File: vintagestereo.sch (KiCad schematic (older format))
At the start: 62 parts, among them J1 Conn_01x08_Male, U1 TL074, U2 TL074

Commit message: autosync
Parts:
- added U?: RDA5807M, symbol AA-ROBSCH:RDA5807M
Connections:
- net labels added: VDD
- wire segments 71 -> 74
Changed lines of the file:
@@
 L power:+5V #PWR?
 U 1 1 609BDE55
-P 10750 4050
-F 0 "#PWR?" H 10750 3900 50  0001 C CNN
-F 1 "+5V" V 10765 4178 50  0000 L CNN
-F 2 "" H 10750 4050 50  0001 C CNN
-F 3 "" H 10750 4050 50  0001 C CNN
-	1    10750 4050
+P 10800 4050
+F 0 "#PWR?" H 10800 3900 50  0001 C CNN
+F 1 "+5V" V 10815 4178 50  0000 L CNN
+F 2 "" H 10800 4050 50  0001 C CNN
+F 3 "" H 10800 4050 50  0001 C CNN
+	1    10800 4050
 	0    1    1    0
 $EndComp
@@
 Text GLabel 8900 5500 0    50   Input ~ 0
 Amp-R
+Text GLabel 2300 3650 3    50   Output ~ 0
+Pre-AL
+Text GLabel 2200 3650 3    50   Output ~ 0
+Pre-AR
+$Comp
+L power:GND #PWR?
+U 1 1 609E4103
+P 2300 2850
+F 0 "#PWR?" H 2300 2600 50  0001 C CNN
+F 1 "GND" H 2305 2677 50  0000 C CNN
+F 2 "" H 2300 2850 50  0001 C CNN
+F 3 "" H 2300 2850 50  0001 C CNN
+	1    2300 2850
+	-1   0    0    1
+$EndComp
+$Comp
+L power:GND #PWR?
+U 1 1 609E6149
+P 2100 2850
+F 0 "#PWR?" H 2100 2600 50  0001 C CNN
+F 1 "GND" H 2105 2677 50  0000 C CNN
+F 2 "" H 2100 2850 50  0001 C CNN
+F 3 "" H 2100 2850 50  0001 C CNN
+	1    2100 2850
+	-1   0    0    1
+$EndComp
+$Comp
+L power:GND #PWR?
+U 1 1 609E6DD9
+P 2100 3650
+F 0 "#PWR?" H 2100 3400 50  0001 C CNN
+F 1 "GND" H 2105 3477 50  0000 C CNN
+F 2 "" H 2100 3650 50  0001 C CNN
+F 3 "" H 2100 3650 50  0001 C CNN
+	1    2100 3650
+	1    0    0    -1
+$EndComp
+Wire Wire Line
+	10800 4050 10750 4050
+Connection ~ 10750 4050
+Wire Wire Line
+	10750 4050 10750 4200
+Wire Wire Line
+	10750 4200 10850 4200
+Text GLabel 10850 4200 2    50   Output Italic 0
+VDD
+Text GLabel 2000 3650 3    50   Input Italic 0
+VDD
+$Comp
+L AA-ROBSCH:RDA5807M U?
+U 1 1 609DFFD6
+P 2050 3200
+F 0 "U?" H 2378 3196 50  0000 L CNN
+F 1 "RDA5807M" H 2378 3105 50  0000 L CNN
+F 2 "" H 2000 3300 50  0001 C CNN
+F 3 "" H 2000 3300 50  0001 C CNN
+	1    2050 3200
+	1    0    0    -1
+$EndComp
 $EndSCHEMATC

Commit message: autosync
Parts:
- removed C? (x12): .1uf, symbol Device:CP
- removed C? (x2): 100uf, symbol Device:CP
- removed C? (x6): 10uf, symbol Device:CP
- removed R? (x6): 1K, symbol Device:R
- removed R? (x12): 47K, symbol Device:R
- removed R? (x6): 100K, symbol Device:R
- removed R? (x2): 10R, symbol Device:R
- removed RV? (x5): 10K A, symbol Device:R_POT_Dual_Separate
- removed unit 5 of U1
- removed unit 3 of U1
- removed unit 4 of U1
- removed unit 2 of U1
- removed U2: TL074, symbol Amplifier_Operational:TL074
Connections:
- net labels added: Pre-CL, Pre-CR
- wire segments 74 -> 20

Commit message: autosync
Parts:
- removed RV?: 10K A, symbol Device:R_POT_Dual_Separate
- added A?: Arduino_Nano_v3.x, Module:Arduino_Nano, symbol MCU_Module:Arduino_Nano_v3.x
- added J? (x2): Conn_01x02_Female, symbol Connector:Conn_01x02_Female
- added J?: Conn_01x04_Female, symbol Connector:Conn_01x04_Female
- added J?: AudioJack2_Ground, symbol Connector:AudioJack2_Ground
- added RV? (x3): R_POT_Dual, symbol Device:R_POT_Dual
- added SW? (x5): SW_Push, symbol Switch:SW_Push
- added SW?: Rotary_Encoder_Switch, symbol Device:Rotary_Encoder_Switch
- U1: value TL074 -> BLUE MODULE
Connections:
- net +5V: now also J1.6 (Pin_6), R?.2, U1.17 (VCC), U1.22 (VCC), A?.27 (+5V), J?.3 (Pin_3), SW?.2, SW?.2, SW?.2, SW?.2, SW?.2, SW?.S1; no longer U?.7 (SCL)
- net GND: now also A?.29 (GND), A?.4 (GND), J?.2 (Pin_2), J?.4 (Pin_4), J?.G, RV?.3, RV?.3, RV?.3, RV?.6, RV?.6, RV?.6, SW?.C; no longer U?.3 (LOut), U?.8 (N/C)
- net Mute: now also A?.20 (A1)
- net Pre-AL: now also U?.3 (LOut), RV?.1; no longer U?.10 (VCC), U?.12 (X0)
- net Pre-AR: now also U?.2 (ROut), RV?.4; no longer U?.1 (Y0), U?.9 (N/C)
- net Pre-BL: now also RV?.1; no longer U?.14 (X1)
- net Pre-BR: now also RV?.4; no longer U?.5 (Y1)
- net Pre-CL: now also J?.S, RV?.1; no longer U?.15 (X2)
- net Pre-CR: now also J?.T, RV?.4; no longer U?.2 (Y2)
- net at U1.1 (M+): now also J?.2 (Pin_2)
- net Vol+: now reaches U1.11 (VOL+)
- net Vol+: now also A?.12 (D9)
- net VOL-: now reaches U1.12 (VOL-)
- net VOL-: now also A?.13 (D10)
- net Next: now reaches U1.13 (NEXT)
- net Next: now also A?.15 (D12)
- net Prev: now reaches U1.14 (PREV)
- net Prev: now also A?.16 (D13)
- net at U1.2 (M-): now also J?.1 (Pin_1)
- net at U?.5 (Antenna): now also J?.1 (Pin_1)
- net SDA: now reaches U?.6 (SDA)
- net SDA: now also A?.23 (A4), J?.1 (Pin_1)
- removed net VCC: J1.6 (Pin_6), R?.2, U1.22 (VCC)
- new net Intrp1: A?.5 (D2), SW?.A
- new net Intrp2: A?.6 (D3), SW?.B
- new net Pause: A?.14 (D11)
- new net SCL: A?.24 (A5), J?.2 (Pin_2), U?.7 (SCL)
- new net Src-AL: RV?.2, U?.12 (X0)
- new net Src-AR: RV?.5, U?.1 (Y0)
- new net Src-BL: RV?.2, U?.14 (X1)
- new net Src-BR: RV?.5, U?.5 (Y1)
- new net Src-CL: RV?.2, U?.15 (X2)
- new net Src-CR: RV?.5, U?.2 (Y2)
- new net Sw1: A?.7 (D4), SW?.1
- new net Sw2: A?.8 (D5), SW?.1
- new net Sw3: A?.9 (D6), SW?.1
- new net Sw4: A?.10 (D7), SW?.1
- new net Sw5: A?.11 (D8), SW?.1
- new net Sw6: A?.19 (A0), SW?.S2
- new net VDD: A?.17 (3V3), U?.10 (VCC)
- no-connect marks 0 -> 14

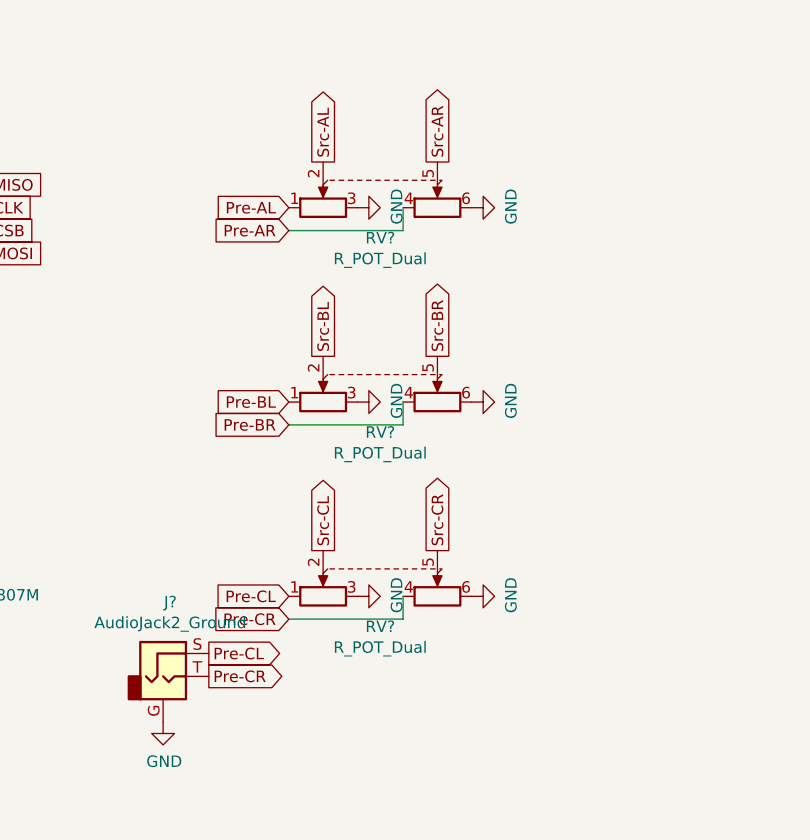
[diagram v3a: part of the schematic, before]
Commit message: swap pots
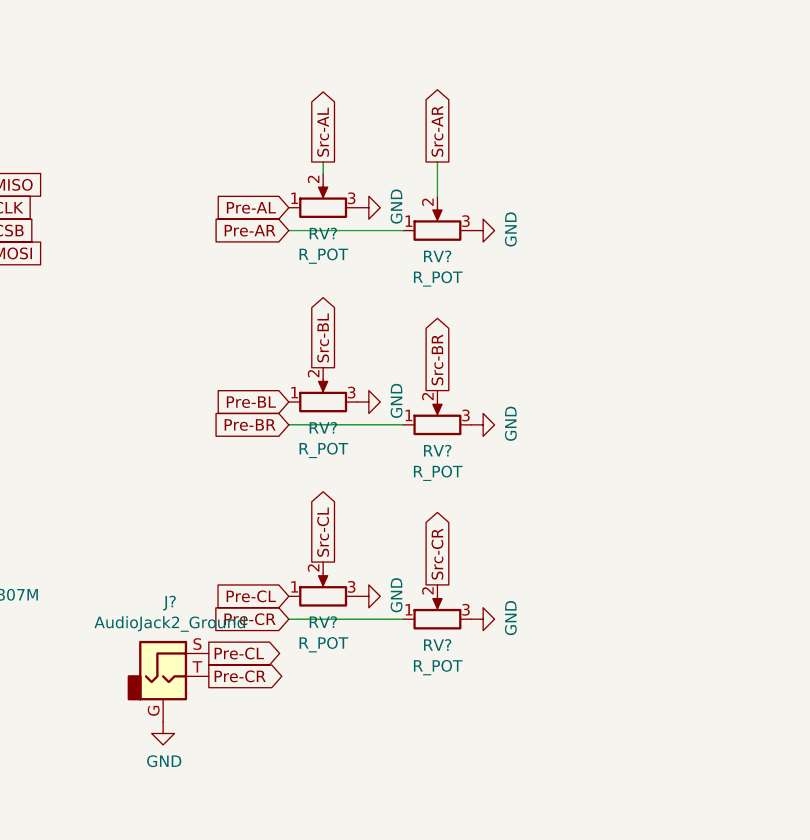
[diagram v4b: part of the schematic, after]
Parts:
- removed RV? (x3): R_POT_Dual, symbol Device:R_POT_Dual
- added RV? (x6): R_POT, symbol Device:R_POT
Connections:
- net GND: now also RV?.3, RV?.3, RV?.3, RV?.3, RV?.3, RV?.3
- net Pre-AL: now also RV?.1
- net Pre-AR: now also RV?.1
- net Pre-BL: now also RV?.1
- net Pre-BR: now also RV?.1
- net Pre-CL: now also RV?.1
- net Pre-CR: now also RV?.1
- net Src-AL: now also RV?.2
- net Src-AR: now also RV?.2
- net Src-BL: now also RV?.2
- net Src-BR: now also RV?.2
- net Src-CL: now also RV?.2
- net Src-CR: now also RV?.2
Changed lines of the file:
@@
 Text GLabel 3850 2450 0    50   Input ~ 0
 Pre-BL
-Text GLabel 4500 2250 1    50   Output ~ 0
-Src-BR
 Text GLabel 3850 2550 0    50   Input ~ 0
 Pre-BR
 Text GLabel 3850 3400 0    50   Input ~ 0
 Pre-CR
-Text GLabel 4500 3100 1    50   Output ~ 0
+Text GLabel 4500 3250 1    50   Output ~ 0
 Src-CR
-Text GLabel 4000 3100 1    50   Output ~ 0
+Text GLabel 4000 3150 1    50   Output ~ 0
 Src-CL
 Text GLabel 3850 3300 0    50   Input ~ 0
@@
 	1    0    0    -1
 $EndComp
-Text GLabel 4000 2250 1    50   Output ~ 0
+Text GLabel 4000 2300 1    50   Output ~ 0
 Src-BL
 Text GLabel 4000 1400 1    50   Output ~ 0
@@
 Pre-AL
 $Comp
-L Device:R_POT_Dual RV?
-U 1 1 60A239E4
-P 4250 1500
-F 0 "RV?" H 4250 1267 50  0000 C CNN
-F 1 "R_POT_Dual" H 4250 1176 50  0000 C CNN
-F 2 "" H 4500 1425 50  0001 C CNN
-F 3 "~" H 4500 1425 50  0001 C CNN
-	1    4250 1500
-	1    0    0    -1
-$EndComp
-Wire Wire Line
-	3850 1700 4350 1700
-Wire Wire Line
-	4350 1700 4350 1600
-$Comp
-L power:GND #PWR?
-U 1 1 60A271AB
-P 4150 1600
-F 0 "#PWR?" H 4150 1350 50  0001 C CNN
-F 1 "GND" H 4155 1427 50  0000 C CNN
-F 2 "" H 4150 1600 50  0001 C CNN
-F 3 "" H 4150 1600 50  0001 C CNN
-	1    4150 1600
-	0    -1   -1   0
-$EndComp
-$Comp
 L power:GND #PWR?
 U 1 1 60A28046
-P 4650 1600
-F 0 "#PWR?" H 4650 1350 50  0001 C CNN
-F 1 "GND" H 4655 1427 50  0000 C CNN
-F 2 "" H 4650 1600 50  0001 C CNN
-F 3 "" H 4650 1600 50  0001 C CNN
-	1    4650 1600
-	0    -1   -1   0
-$EndComp
-$Comp
-L Device:R_POT_Dual RV?
-U 1 1 60A29E30
-P 4250 2350
-F 0 "RV?" H 4250 2117 50  0000 C CNN
-F 1 "R_POT_Dual" H 4250 2026 50  0000 C CNN
-F 2 "" H 4500 2275 50  0001 C CNN
-F 3 "~" H 4500 2275 50  0001 C CNN
-	1    4250 2350
-	1    0    0    -1
-$EndComp
-Wire Wire Line
-	3850 2550 4350 2550
-Wire Wire Line
-	4350 2550 4350 2450
-$Comp
-L power:GND #PWR?
-U 1 1 60A2A0C8
-P 4150 2450
-F 0 "#PWR?" H 4150 2200 50  0001 C CNN
-F 1 "GND" H 4155 2277 50  0000 C CNN
-F 2 "" H 4150 2450 50  0001 C CNN
-F 3 "" H 4150 2450 50  0001 C CNN
-	1    4150 2450
-	0    -1   -1   0
-$EndComp
-$Comp
-L power:GND #PWR?
-U 1 1 60A2A0D2
-P 4650 2450
-F 0 "#PWR?" H 4650 2200 50  0001 C CNN
-F 1 "GND" H 4655 2277 50  0000 C CNN
-F 2 "" H 4650 2450 50  0001 C CNN
-F 3 "" H 4650 2450 50  0001 C CNN
-	1    4650 2450
-	0    -1   -1   0
-$EndComp
-$Comp
-L Device:R_POT_Dual RV?
-U 1 1 60A2F48E
-P 4250 3200
-F 0 "RV?" H 4250 2967 50  0000 C CNN
-F 1 "R_POT_Dual" H 4250 2876 50  0000 C CNN
-F 2 "" H 4500 3125 50  0001 C CNN
-F 3 "~" H 4500 3125 50  0001 C CNN
-	1    4250 3200
-	1    0    0    -1
-$EndComp
-Wire Wire Line
-	3850 3400 4350 3400
-Wire Wire Line
-	4350 3400 4350 3300
-$Comp
-L power:GND #PWR?
-U 1 1 60A315D0
-P 4650 3300
-F 0 "#PWR?" H 4650 3050 50  0001 C CNN
-F 1 "GND" H 4655 3127 50  0000 C CNN
-F 2 "" H 4650 3300 50  0001 C CNN
-F 3 "" H 4650 3300 50  0001 C CNN
-	1    4650 3300
-	0    -1   -1   0
-$EndComp
-$Comp
-L power:GND #PWR?
-U 1 1 60A31BDA
-P 4150 3300
-F 0 "#PWR?" H 4150 3050 50  0001 C CNN
-F 1 "GND" H 4155 3127 50  0000 C CNN
-F 2 "" H 4150 3300 50  0001 C CNN
-F 3 "" H 4150 3300 50  0001 C CNN
-	1    4150 3300
+P 4650 1700
+F 0 "#PWR?" H 4650 1450 50  0001 C CNN
+F 1 "GND" H 4655 1527 50  0000 C CNN
+F 2 "" H 4650 1700 50  0001 C CNN
+F 3 "" H 4650 1700 50  0001 C CNN
+	1    4650 1700
 	0    -1   -1   0
 $EndComp
@@
 Text GLabel 7700 2200 2    50   Output Italic 0
 Mute
+$Comp
+L Device:R_POT RV?
+U 1 1 60A8ABB1
+P 4000 1600
+F 0 "RV?" V 3885 1600 50  0000 C CNN
+F 1 "R_POT" V 3794 1600 50  0000 C CNN
+F 2 "" H 4000 1600 50  0001 C CNN
+F 3 "~" H 4000 1600 50  0001 C CNN
+	1    4000 1600
+	0    -1   -1   0
+$EndComp
+$Comp
+L Device:R_POT RV?
+U 1 1 60A8BA8A
+P 4500 1700
+F 0 "RV?" V 4385 1700 50  0000 C CNN
+F 1 "R_POT" V 4294 1700 50  0000 C CNN
+F 2 "" H 4500 1700 50  0001 C CNN
+F 3 "~" H 4500 1700 50  0001 C CNN
+	1    4500 1700
+	0    -1   -1   0
+$EndComp
+$Comp
+L power:GND #PWR?
+U 1 1 60A8E36E
+P 4150 1600
+F 0 "#PWR?" H 4150 1350 50  0001 C CNN
+F 1 "GND" H 4155 1427 50  0000 C CNN
+F 2 "" H 4150 1600 50  0001 C CNN
+F 3 "" H 4150 1600 50  0001 C CNN
+	1    4150 1600
+	0    -1   -1   0
+$EndComp
+Wire Wire Line
+	3850 1700 4350 1700
+Wire Wire Line
+	4500 1550 4500 1400
+Wire Wire Line
+	4000 1450 4000 1400
+$Comp
+L Device:R_POT RV?
+U 1 1 60A93929
+P 4500 2550
+F 0 "RV?" V 4385 2550 50  0000 C CNN
+F 1 "R_POT" V 4294 2550 50  0000 C CNN
+F 2 "" H 4500 2550 50  0001 C CNN
+F 3 "~" H 4500 2550 50  0001 C CNN
+	1    4500 2550
+	0    -1   -1   0
+$EndComp
+$Comp
+L Device:R_POT RV?
+U 1 1 60A925E0
+P 4000 2450
+F 0 "RV?" V 3885 2450 50  0000 C CNN
+F 1 "R_POT" V 3794 2450 50  0000 C CNN
+F 2 "" H 4000 2450 50  0001 C CNN
+F 3 "~" H 4000 2450 50  0001 C CNN
+	1    4000 2450
+	0    -1   -1   0
+$EndComp
+$Comp
+L power:GND #PWR?
+U 1 1 60A2A0D2
+P 4650 2550
+F 0 "#PWR?" H 4650 2300 50  0001 C CNN
+F 1 "GND" H 4655 2377 50  0000 C CNN
+F 2 "" H 4650 2550 50  0001 C CNN
+F 3 "" H 4650 2550 50  0001 C CNN
+	1    4650 2550
+	0    -1   -1   0
+$EndComp
+$Comp
+L power:GND #PWR?
+U 1 1 60A2A0C8
+P 4150 2450
+F 0 "#PWR?" H 4150 2200 50  0001 C CNN
+F 1 "GND" H 4155 2277 50  0000 C CNN
+F 2 "" H 4150 2450 50  0001 C CNN
+F 3 "" H 4150 2450 50  0001 C CNN
+	1    4150 2450
+	0    -1   -1   0
+$EndComp
+Wire Wire Line
+	3850 2550 4350 2550
+Text GLabel 4500 2400 1    50   Output ~ 0
+Src-BR
+$Comp
+L Device:R_POT RV?
+U 1 1 60A98E1F
+P 4500 3400
+F 0 "RV?" V 4385 3400 50  0000 C CNN
+F 1 "R_POT" V 4294 3400 50  0000 C CNN
+F 2 "" H 4500 3400 50  0001 C CNN
+F 3 "~" H 4500 3400 50  0001 C CNN
+	1    4500 3400
+	0    -1   -1   0
+$EndComp
+$Comp
+L Device:R_POT RV?
+U 1 1 60A99217
+P 4000 3300
+F 0 "RV?" V 3885 3300 50  0000 C CNN
+F 1 "R_POT" V 3794 3300 50  0000 C CNN
+F 2 "" H 4000 3300 50  0001 C CNN
+F 3 "~" H 4000 3300 50  0001 C CNN
+	1    4000 3300
+	0    -1   -1   0
+$EndComp
+$Comp
+L power:GND #PWR?
+U 1 1 60A99221
+P 4650 3400
+F 0 "#PWR?" H 4650 3150 50  0001 C CNN
+F 1 "GND" H 4655 3227 50  0000 C CNN
+F 2 "" H 4650 3400 50  0001 C CNN
+F 3 "" H 4650 3400 50  0001 C CNN
+	1    4650 3400
+	0    -1   -1   0
+$EndComp
+$Comp
+L power:GND #PWR?
+U 1 1 60A9922B
+P 4150 3300
+F 0 "#PWR?" H 4150 3050 50  0001 C CNN
+F 1 "GND" H 4155 3127 50  0000 C CNN
+F 2 "" H 4150 3300 50  0001 C CNN
+F 3 "" H 4150 3300 50  0001 C CNN
+	1    4150 3300
+	0    -1   -1   0
+$EndComp
+Wire Wire Line
+	3850 3400 4350 3400
 $EndSCHEMATC

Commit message: V0.0.2 Schematic Rough Play/pause
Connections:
- net Pause: now also A?.21 (A2), U1.15 (PlayPause)
- no-connect marks 14 -> 12
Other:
- note added: "VintageStereo V0.0.2"
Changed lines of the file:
@@
 Text GLabel 6700 2400 0    50   Output ~ 0
 Vol+
-NoConn ~ 1900 1100
 NoConn ~ 1800 1100
 Text GLabel 6700 1700 0    50   Input ~ 0
@@
 NoConn ~ 6700 1500
 NoConn ~ 6700 1600
-NoConn ~ 7700 2300
 NoConn ~ 7700 2400
 NoConn ~ 7700 2700
@@
 Wire Wire Line
 	3850 3400 4350 3400
+Text GLabel 7700 2300 2    50   Output Italic 0
+Pause
+Text GLabel 1900 1100 1    50   Input Italic 0
+Pause
+Text Notes 7100 6700 0    50   ~ 0
+VintageStereo V0.0.2
 $EndSCHEMATC
